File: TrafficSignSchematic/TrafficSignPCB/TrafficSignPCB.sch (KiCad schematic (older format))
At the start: 25 parts, among them J1 IDC connector, J2 3.96mm pitch 4-pin polarized 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, U1 ATmega328P-PU, U2 SIM800L, Y1 16MHz

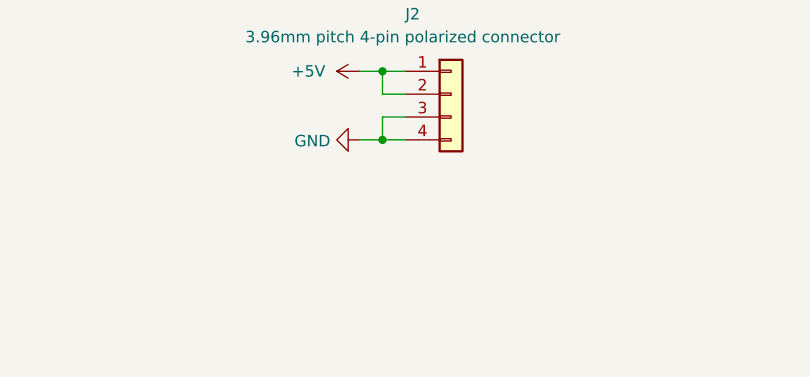
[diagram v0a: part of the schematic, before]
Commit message: Placed elements on PCB (Not final)
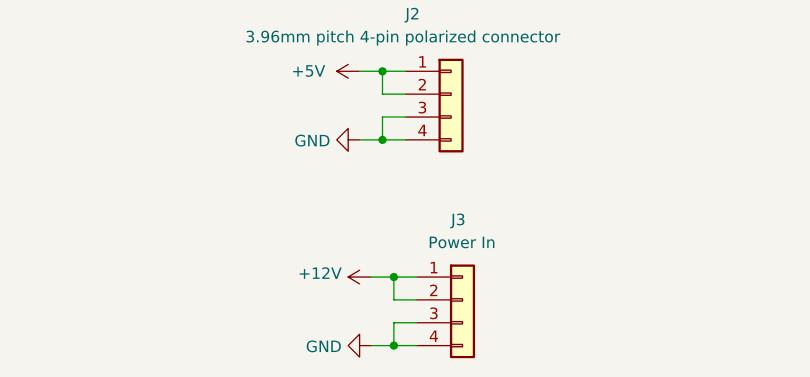
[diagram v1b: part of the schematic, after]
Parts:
- added J3: Power In, Connector_Molex:Molex_KK-396_A-41791-0004_1x04_P3.96mm_Vertical, symbol Connector_Generic:Conn_01x04
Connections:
- wire segments 154 -> 162
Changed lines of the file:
@@
 Wire Wire Line
 	2400 2500 3550 2500
-$Comp
-L power:GND #PWR0112
-U 1 1 5E1132F7
-P 3800 2450
-F 0 "#PWR0112" H 3800 2200 50  0001 C CNN
-F 1 "GND" V 3805 2322 50  0000 R CNN
-F 2 "" H 3800 2450 50  0001 C CNN
-F 3 "" H 3800 2450 50  0001 C CNN
-	1    3800 2450
-	0    -1   -1   0
-$EndComp
 Wire Wire Line
 	2400 2800 2450 2800
@@
 NoConn ~ 3150 4000
 NoConn ~ 3150 4400
+$Comp
+L power:GND #PWR0112
+U 1 1 5E1132F7
+P 3800 2450
+F 0 "#PWR0112" H 3800 2200 50  0001 C CNN
+F 1 "GND" V 3805 2322 50  0000 R CNN
+F 2 "" H 3800 2450 50  0001 C CNN
+F 3 "" H 3800 2450 50  0001 C CNN
+	1    3800 2450
+	0    -1   -1   0
+$EndComp
+$Comp
+L Connector_Generic:Conn_01x04 J3
+U 1 1 5E26C348
+P 4850 6500
+F 0 "J3" H 4800 6850 50  0000 L CNN
+F 1 "Power In" H 4700 6750 50  0000 L CNN
+F 2 "Connector_Molex:Molex_KK-396_A-41791-0004_1x04_P3.96mm_Vertical" H 4850 6500 50  0001 C CNN
+F 3 "https://store.comet.bg/Catalogue/Product/25223/" H 4850 6500 50  0001 C CNN
+	1    4850 6500
+	1    0    0    -1
+$EndComp
+Wire Wire Line
+	4650 6400 4550 6400
+Wire Wire Line
+	4650 6500 4550 6500
+Wire Wire Line
+	4650 6600 4550 6600
+Wire Wire Line
+	4650 6700 4550 6700
+Wire Wire Line
+	4550 6600 4550 6700
+Wire Wire Line
+	4550 6700 4450 6700
+Connection ~ 4550 6700
+Wire Wire Line
+	4550 6500 4550 6400
+Wire Wire Line
+	4550 6400 4450 6400
+Connection ~ 4550 6400
+$Comp
+L power:GND #PWR0116
+U 1 1 5E26C35E
+P 4450 6700
+F 0 "#PWR0116" H 4450 6450 50  0001 C CNN
+F 1 "GND" V 4455 6572 50  0000 R CNN
+F 2 "" H 4450 6700 50  0001 C CNN
+F 3 "" H 4450 6700 50  0001 C CNN
+	1    4450 6700
+	0    1    1    0
+$EndComp
+$Comp
+L power:+12V #PWR?
+U 1 1 5E2A224F
+P 4450 6400
+F 0 "#PWR?" H 4450 6250 50  0001 C CNN
+F 1 "+12V" V 4465 6528 50  0000 L CNN
+F 2 "" H 4450 6400 50  0001 C CNN
+F 3 "" H 4450 6400 50  0001 C CNN
+	1    4450 6400
+	0    -1   -1   0
+$EndComp
 $EndSCHEMATC

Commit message: Element placement v2
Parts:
- U2: symbol SIM800L:SIM800L -> TrafficSignPCB-rescue:SIM800L-SIM800L
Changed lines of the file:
@@
 NoConn ~ 6000 2750
 $Comp
-L SIM800L:SIM800L U2
+L TrafficSignPCB-rescue:SIM800L-SIM800L U2
 U 1 1 5DF831F1
 P 5350 2500

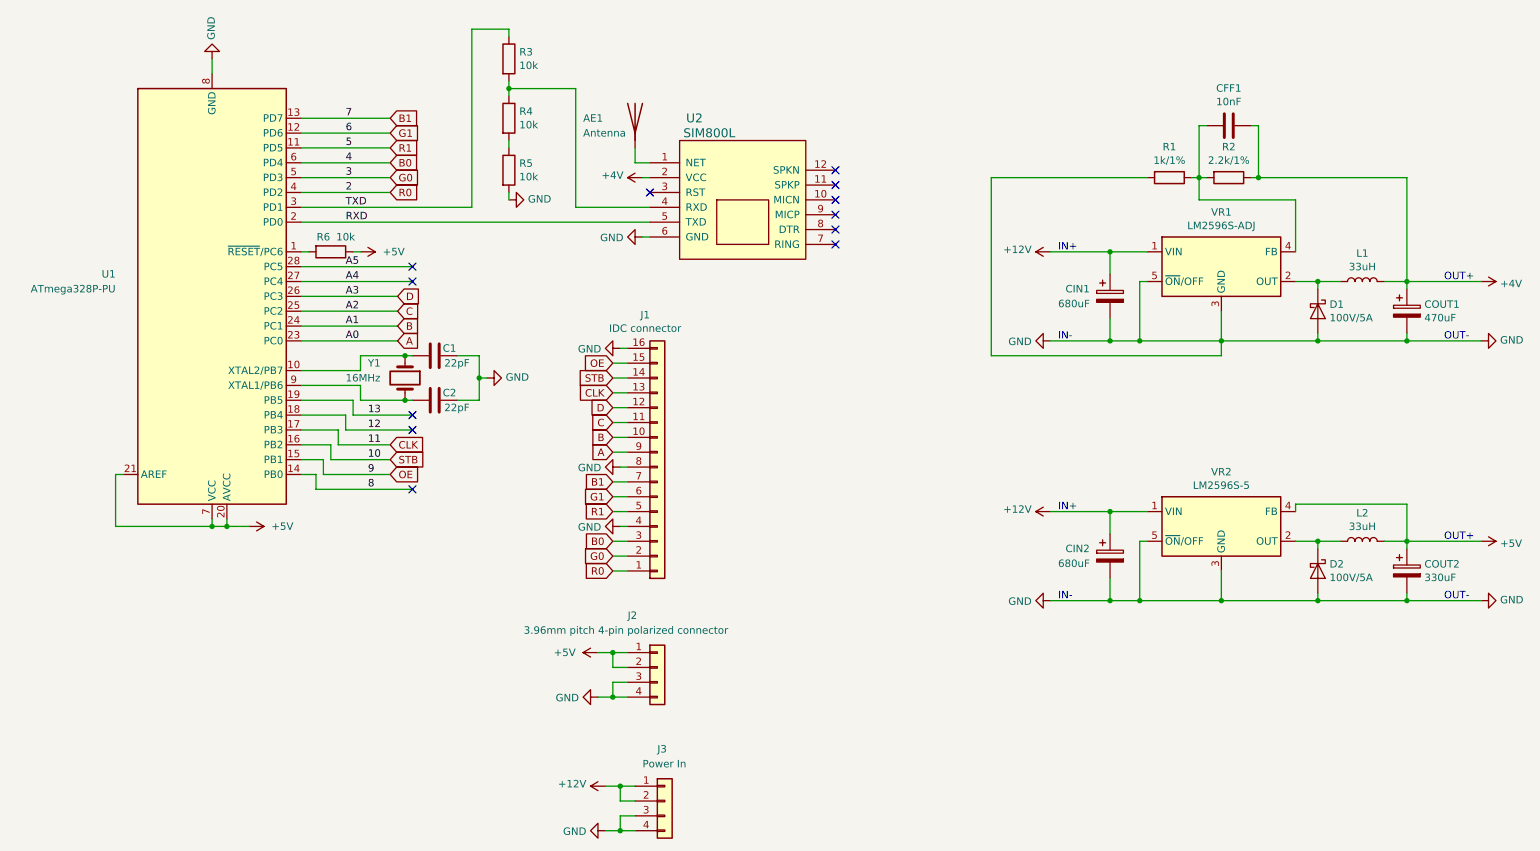
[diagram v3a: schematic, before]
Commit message: Added missing capacitors, changed converter output capacitors to Low ESR
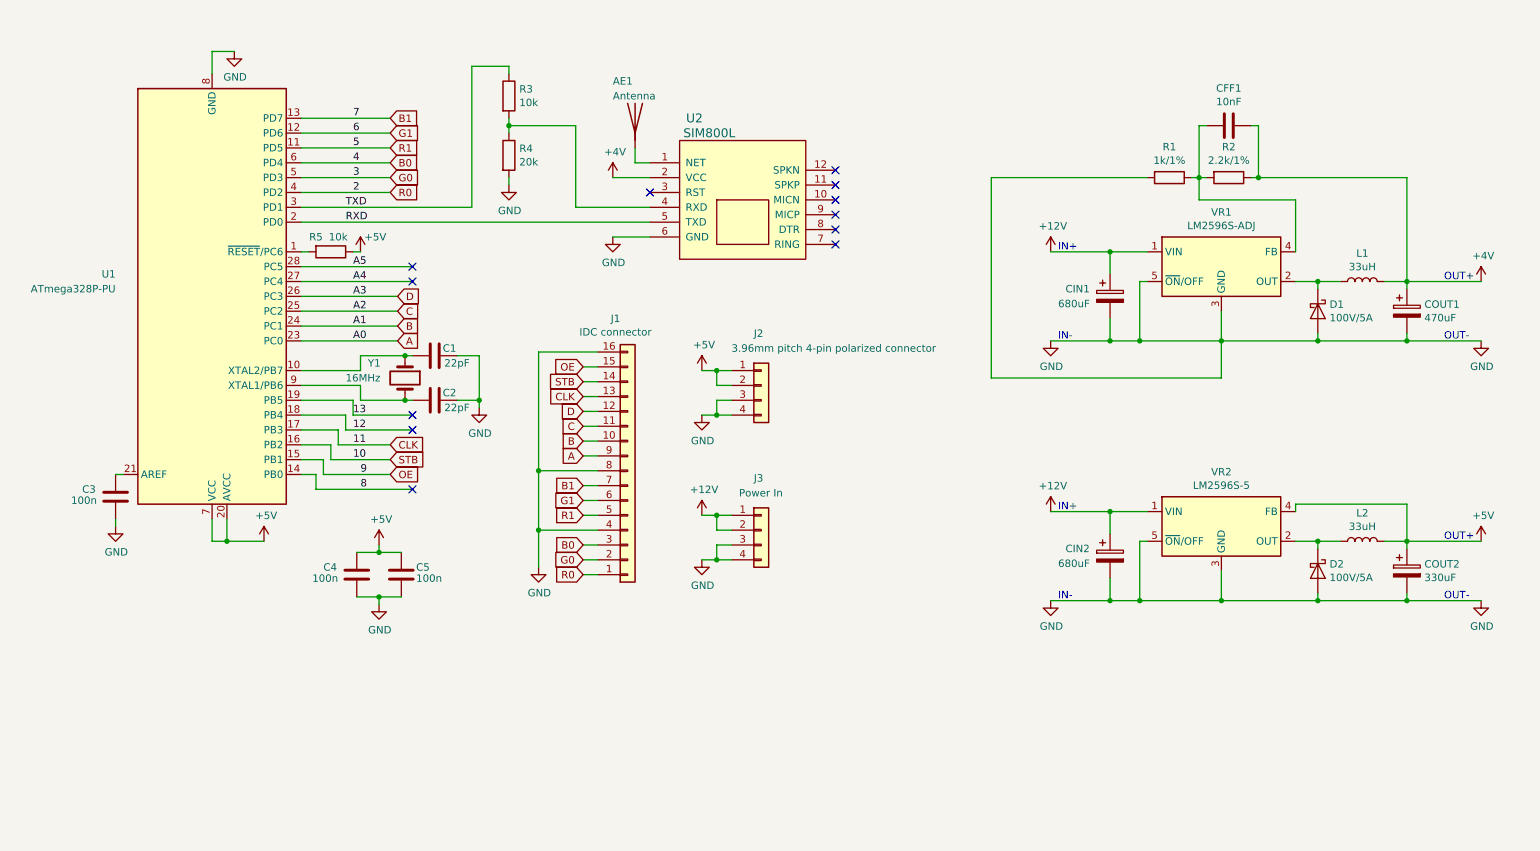
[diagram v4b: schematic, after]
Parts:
- removed R5: 10k, Resistor_THT:R_Axial_DIN0204_L3.6mm_D1.6mm_P7.62mm_Horizontal, symbol Device:R
- added C3, C4, C5: 100n, Capacitor_THT:C_Disc_D4.3mm_W1.9mm_P5.00mm, symbol Device:C
- COUT1, COUT2: footprint Capacitor_THT:CP_Radial_D10.0mm_P5.00mm -> Capacitor_THT:CP_Radial_D8.0mm_P3.50mm
- R4: value 10k -> 20k
- renumbered R6 to R5
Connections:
- net +5V: now also C4.1, C5.1; no longer U1.21 (AREF)
- net GND: now also R4.2, C3.2, C4.2, C5.2
- new net: C3.1, U1.21 (AREF)
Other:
- moved on the sheet: J1, J2, J3, R3, R4
